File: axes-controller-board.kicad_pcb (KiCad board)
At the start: 2 copper layers, 135 parts, among them IC1 TPS5450QDDARQ1, IC2 ACS37800KMACTR-030B3-SPI, IC3 ACS37800KMACTR-030B3-SPI, IC4 ACS37800KMACTR-030B3-SPI, IC5 STM32H723ZGT6, J1 Conn_ST_STDC14, J10 Conn_01x08, J11 Conn_01x04, J12 Conn_01x08, J13 Conn_01x04, J14 Conn_01x08, J15 Conn_01x08, J16 Conn_01x04, J17 Conn_01x08, J18 Conn_01x08, J19 Conn_01x04, J2 Conn_01x03, J20 Conn_01x08, J21 Conn_01x08, J22 Conn_01x04, J23 Conn_01x08, J24 Conn_01x08, J25 Conn_01x04, J26 Conn_01x08, J27 Raspberry_Pi_2_3, J28 DC1, J29 DC2, J3 Conn_01x03, J30 DC3, J31 Conn_01x08, J32 Conn_01x08, J4 Conn_01x03, J5 DRIVER, J6 NTC, J7 DRIVER, J8 NTC, J9 Conn_01x08, SW1 RESET, U1 LM1117MP-3.3, U3 UA9637A, U5 UA9637A, U7 UA9637A, Y1 16MHz

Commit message: feat: setup groups pcb
steppers, micro, clock, current sensor - connector
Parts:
- moved C51 169.3 mm to (106.6, -64.5), turned to 90 degrees
- moved C53 169.3 mm to (152.6, -63.9), turned to 90 degrees
- moved C52 168.2 mm to (129.6, -64.2), turned to 90 degrees
- moved C11 163.5 mm to (217.2, 0.21), turned to -90 degrees
- moved C10 162.4 mm to (219.2, 0.21), turned to -90 degrees
- moved C15 161.6 mm to (213.8, -14.1), turned to -90 degrees
- moved L2 156.1 mm to (228.4, -5.54)
- moved R9 155.6 mm to (210.8, -14.1), turned to 90 degrees
- moved J16 155.5 mm to (149.3, -69.0), turned to 90 degrees
- moved R8 154.3 mm to (212.3, -14.1), turned to -90 degrees
- moved U1 152.9 mm to (218.4, 21.7)
- moved J13 152.3 mm to (125.9, -68.8), turned to 90 degrees
- moved J11 151.4 mm to (103.2, -68.6), turned to 90 degrees
- moved C13 150.1 mm to (212.5, -3.54), turned to 180 degrees
- moved C12 147.0 mm to (215.4, 0.06), turned to -90 degrees
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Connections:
- C13 pad 1: Net-(IC1-PH) -> /IBC
- C13 pad 2: Net-(D3-K) -> Net-(IC1-BOOT)
- D3 pad 1: Net-(D3-K) -> /IBC
- IC1 pad 1: Net-(D3-K) -> Net-(IC1-BOOT)
- IC1 pad 8: Net-(IC1-PH) -> /IBC
- J10 pad 1: GND -> +12V
- J10 pad 2: +3V3 -> GND
- J10 pad 7: GND -> +3V3
- J10 pad 8: +12V -> GND
- J14 pad 1: GND -> +12V
- J14 pad 2: +3V3 -> GND
- J14 pad 7: GND -> +3V3
- J14 pad 8: +12V -> GND
- J17 pad 1: GND -> +12V
- J17 pad 2: +3V3 -> GND
- J17 pad 7: GND -> +3V3
- J17 pad 8: +12V -> GND
- J20 pad 1: GND -> +12V
- J20 pad 2: +3V3 -> GND
- J20 pad 7: GND -> +3V3
- J20 pad 8: +12V -> GND
- J23 pad 1: GND -> +12V
- J23 pad 2: +3V3 -> GND
- J23 pad 7: GND -> +3V3
- J23 pad 8: +12V -> GND
- J26 pad 1: GND -> +12V
- J26 pad 2: +3V3 -> GND
- J26 pad 7: GND -> +3V3
- J26 pad 8: +12V -> GND
- J28 pad 1: /Sensors/DC_1_OUT -> /Sensors/DC_1_IN
- J28 pad 2: /Sensors/DC_1_IN -> /Sensors/DC_1_OUT
- J29 pad 1: /Sensors/DC_2_OUT -> /Sensors/DC_2_IN
- J29 pad 2: /Sensors/DC_2_IN -> /Sensors/DC_2_OUT
- J30 pad 1: /Sensors/DC_3_OUT -> /Sensors/DC_3_IN
- J30 pad 2: /Sensors/DC_3_IN -> /Sensors/DC_3_OUT
- L2 pad 1: Net-(D3-K) -> /IBC
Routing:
- net /MCU/OSC_OUT: track 0.00 -> 7.88 mm
- net /MCU/OSC_IN: track 1.81 -> 6.16 mm
- added copper zone on F.Cu, net +12V
- added copper zone on F.Cu, net /IBC
- added copper zone on F.Cu, net /Sensors/DC_1_IN
- added copper zone on F.Cu, net /Sensors/DC_1_OUT
- added copper zone on F.Cu, net /Sensors/DC_2_IN
- added copper zone on F.Cu, net /Sensors/DC_2_OUT
- added copper zone on F.Cu, net /Sensors/DC_3_IN
- added copper zone on F.Cu, net /Sensors/DC_3_OUT
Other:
- board text added: "+3V3"
- board text added: "+5V"

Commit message: fix: missing input power connector
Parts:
- added J33: DC1, TerminalBlock_Phoenix:TerminalBlock_Phoenix_MKDS-1,5-2-5.08_1x02_P5.08mm_Horizontal, F.Cu at (224.7, 6.96)
- moved JP2 148.0 mm to (79.5, -43.2)
- moved C39 108.6 mm to (270.7, 139.2), turned to 180 degrees
- moved C34 93.1 mm to (254.3, 139.1), turned to 180 degrees
- moved C33 80.2 mm to (238.5, 139.1), turned to 180 degrees
- moved J2 76.8 mm to (96.3, 18.9)
- moved J3 76.8 mm to (101.0, 18.9)
- moved J4 76.8 mm to (105.6, 18.9)
- moved C32 28.9 mm to (198.3, 94.3)
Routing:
- net GND: track 35.0 -> 41.5 mm
- net +3V3: track 42.8 -> 48.9 mm

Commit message: feat: sbroglio encoders drivers
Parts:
- moved R50 70.6 mm to (168.0, 170.2), turned to 180 degrees
- moved R49 70.0 mm to (168.0, 167.1), turned to 180 degrees
- moved R38 69.8 mm to (158.0, 156.6), turned to -90 degrees
- moved R52 68.8 mm to (158.2, 170.7), turned to -90 degrees
- moved C45 68.5 mm to (168.0, 171.8), turned to 180 degrees
- moved R51 68.3 mm to (158.2, 167.6), turned to 90 degrees
- moved U7 68.1 mm to (162.7, 169.5)
- moved R39 68.0 mm to (156.4, 156.7), turned to -90 degrees
- moved C44 68.0 mm to (168.0, 168.7), turned to 180 degrees
- moved R53 66.9 mm to (156.7, 170.6), turned to -90 degrees
- moved C49 64.8 mm to (155.1, 170.6), turned to 90 degrees
- moved C42 63.5 mm to (154.9, 156.7), turned to 90 degrees
- moved R40 62.9 mm to (156.4, 153.6), turned to -90 degrees
- moved C54 62.5 mm to (145.9, -76.3)
- moved C55 62.5 mm to (171.8, -76.2)
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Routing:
- net Net-(IC1-VSENSE): track 0.00 -> 19.8 mm
- net Net-(IC1-BOOT): track 0.00 -> 4.65 mm
- net /MCU/MY1_A: track 0.00 -> 3.13 mm
- net /MCU/MY2_B: track 0.00 -> 3.11 mm
- net /MCU/MY2_A: track 0.00 -> 3.11 mm
- net /MCU/MY1_B: track 0.00 -> 3.11 mm
- net /MCU/MX_A: track 0.00 -> 3.10 mm
- net /MCU/MX_B: track 0.00 -> 3.08 mm
- net Net-(U3-OUT1): track 0.00 -> 2.23 mm
- net /Sensors/M1_B-: track 0.00 -> 2.20 mm
- net /Sensors/M2_A+: track 0.00 -> 2.19 mm
- net /Sensors/M3_B-: track 0.00 -> 2.19 mm
- net Net-(U5-OUT1): track 0.00 -> 2.19 mm
- net Net-(U7-OUT1): track 0.00 -> 2.19 mm
- net Net-(U3-OUT2): track 0.00 -> 2.17 mm
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
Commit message: feat: rasp, supply and micro setup on pcb, missing stepper motors connectors
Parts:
- moved D5 240.8 mm to (143.7, 135.3)
- moved R10 240.8 mm to (142.1, 135.3)
- moved R11 240.8 mm to (142.1, 138.4)
- moved D6 240.8 mm to (143.7, 138.4)
- moved J1 233.6 mm to (128.1, 153.3)
- moved SW1 229.0 mm to (117.5, 152.1), turned to 90 degrees
- moved C6 225.9 mm to (120.3, 149.5), turned to 90 degrees
- moved D7 225.1 mm to (120.2, 152.4), turned to -90 degrees
- moved J4 213.7 mm to (257.1, 169.6), turned to 90 degrees
- moved J3 213.7 mm to (262.5, 158.8)
- moved J5 202.3 mm to (331.0, 77.5)
- moved J31 202.3 mm to (310.0, 88.4)
- moved J32 202.3 mm to (310.0, 99.2)
- moved J6 202.3 mm to (321.7, 77.5)
- moved J7 202.3 mm to (335.6, 77.5)
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
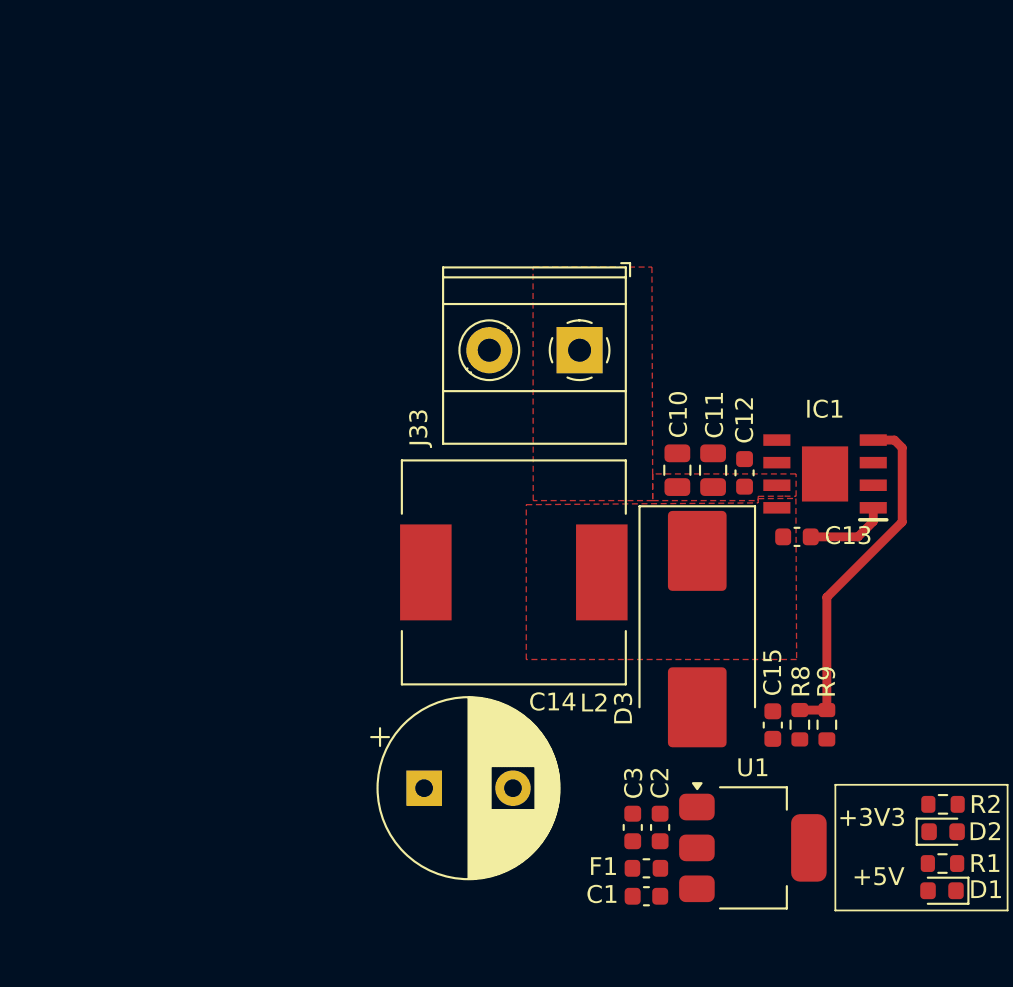
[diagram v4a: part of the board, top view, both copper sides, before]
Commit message: fix: dcdc layout according to datasheet
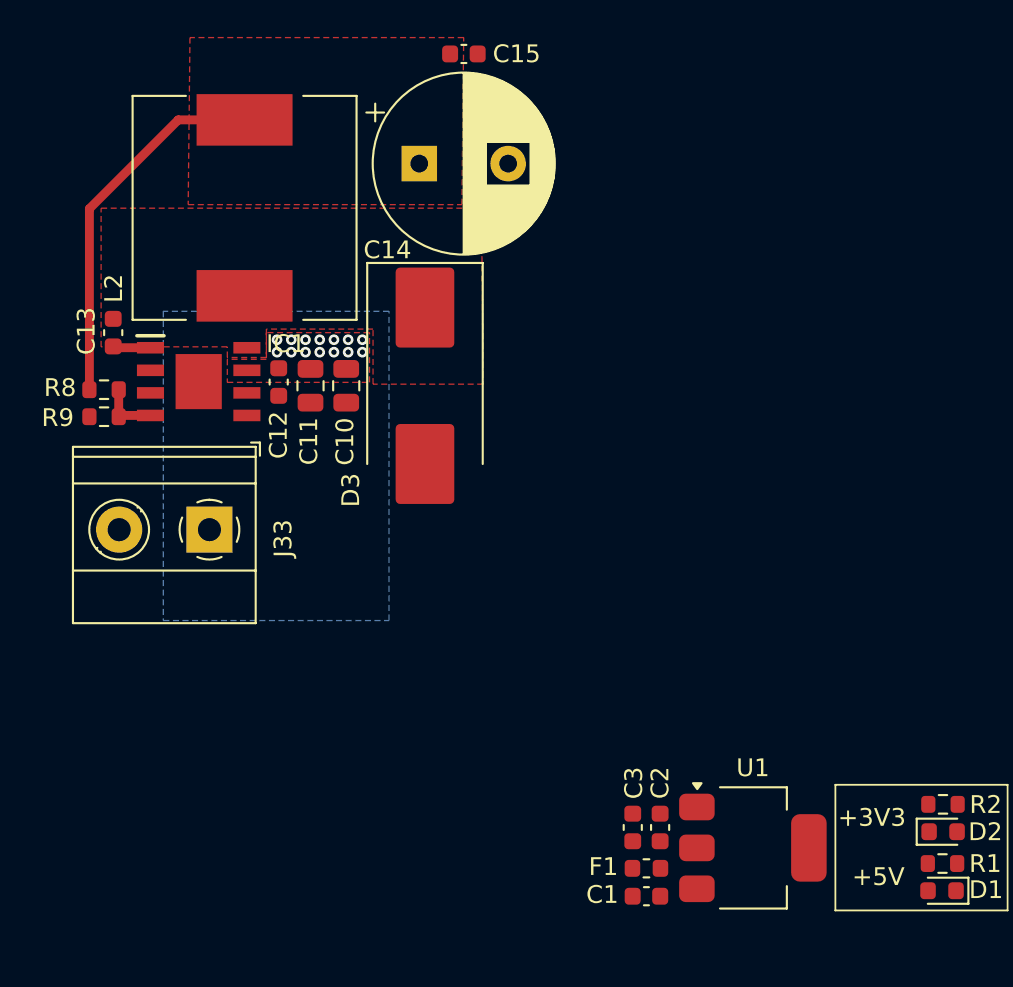
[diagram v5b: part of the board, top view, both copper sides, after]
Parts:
- moved R9 44.2 mm to (41.5, 63.4), turned to 180 degrees
- moved R8 43.4 mm to (41.5, 61.9), turned to 0 degrees
- moved C15 41.6 mm to (61.7, 43.0), turned to 0 degrees
- moved C13 40.1 mm to (42.0, 58.7), turned to -90 degrees
- moved IC1 35.6 mm to (46.8, 61.4), turned to 0 degrees
- moved C14 35.1 mm to (59.2, 49.2)
- moved C12 26.7 mm to (51.3, 61.5), turned to -90 degrees
- moved L2 25.5 mm to (49.4, 51.6), turned to 90 degrees
- moved J33 23.1 mm to (47.4, 69.8)
- moved C11 23.1 mm to (53.1, 61.7), turned to -90 degrees
- moved D3 20.5 mm to (59.5, 61.7)
- moved C10 19.2 mm to (55.1, 61.7), turned to -90 degrees
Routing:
- net +5V: track 0.00 -> 21.0 mm
- net Net-(IC1-VSENSE): track 19.8 -> 3.33 mm
- net Net-(IC1-BOOT): track 4.65 -> 2.13 mm
- net +12V: vias 0 -> 14
- added copper zone on B.Cu, net +12V
- added copper zone on F.Cu, net +5V

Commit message: feat: 3d models and first draft pcb edge cuts
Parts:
- J27: moved to B.Cu
- moved J32 171.5 mm to (145.9, 149.0)
- moved J31 157.0 mm to (165.1, 149.0)
- moved C45 152.9 mm to (182.8, 143.8), turned to 90 degrees
- moved R50 150.9 mm to (184.3, 143.8), turned to 90 degrees
- moved C44 149.0 mm to (185.8, 143.8), turned to 90 degrees
- moved R49 147.1 mm to (187.4, 143.8), turned to 90 degrees
- moved U7 146.6 mm to (185.1, 138.5), turned to -90 degrees
- moved R52 145.5 mm to (183.9, 134.0), turned to 180 degrees
- moved R53 144.7 mm to (183.9, 132.5), turned to 180 degrees
- moved C49 143.9 mm to (183.9, 130.9), turned to 0 degrees
- moved R51 141.6 mm to (186.9, 134.0), turned to 0 degrees
- moved R54 140.7 mm to (186.9, 132.5), turned to 180 degrees
- moved C47 140.6 mm to (188.7, 136.3), turned to -90 degrees
- moved C50 139.9 mm to (186.9, 130.9), turned to 180 degrees
- moved C38 137.2 mm to (194.9, 143.8), turned to 90 degrees
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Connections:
- J33 pad 1: +12V -> GND
- J33 pad 2: GND -> +12V
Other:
- board outline added: 184.6 x 102.9 mm

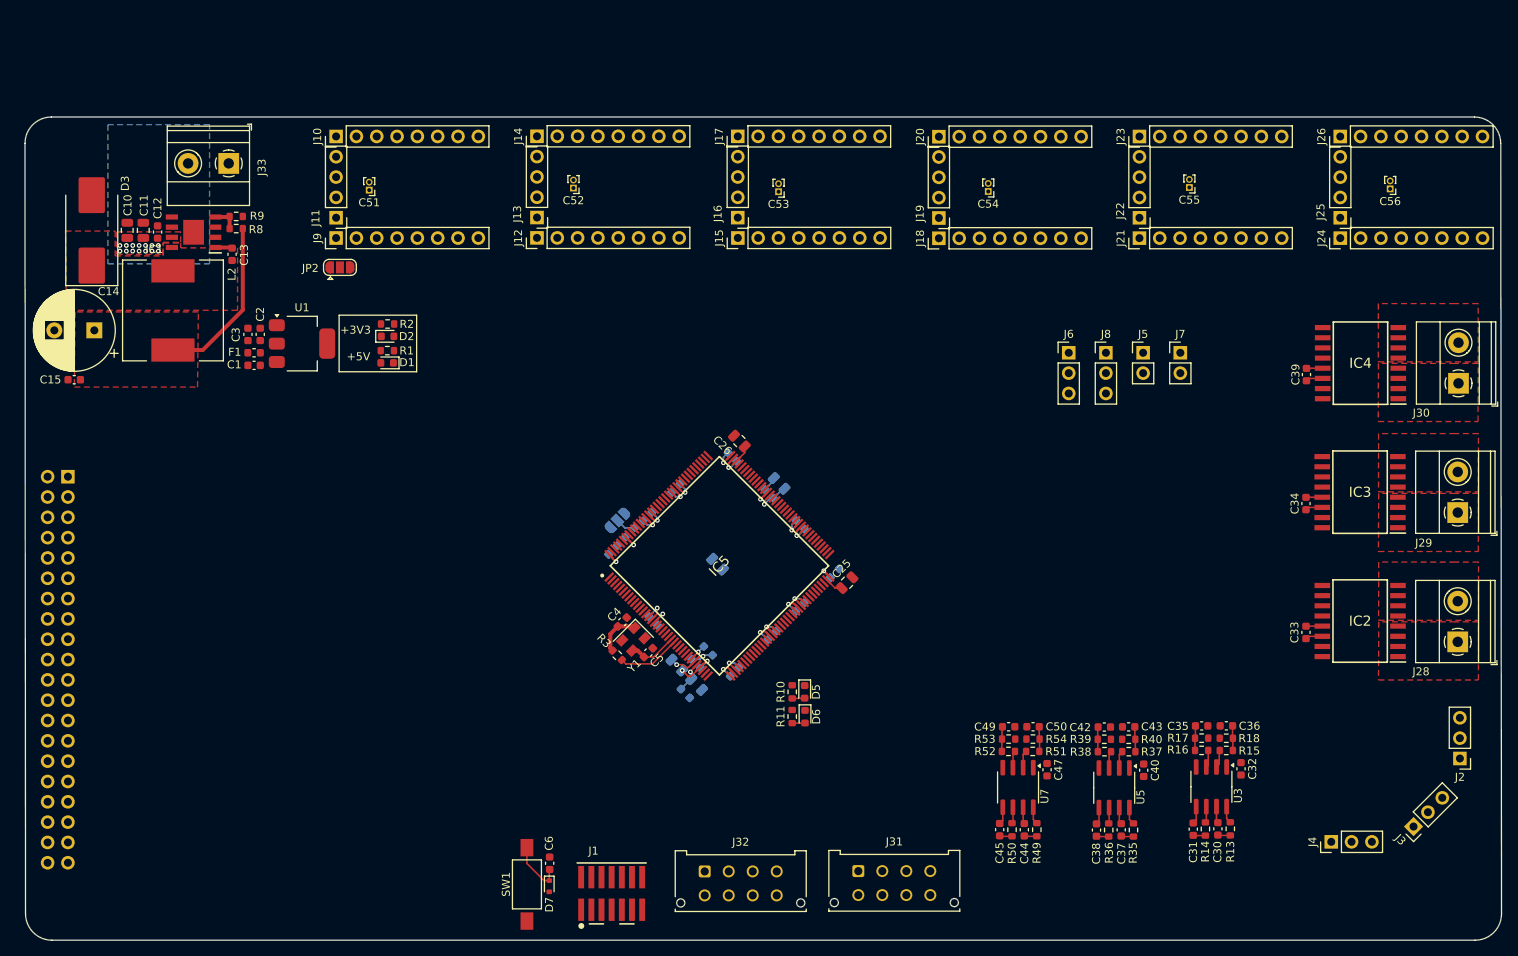
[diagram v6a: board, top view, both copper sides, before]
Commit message: fix: connectors and pcb layout
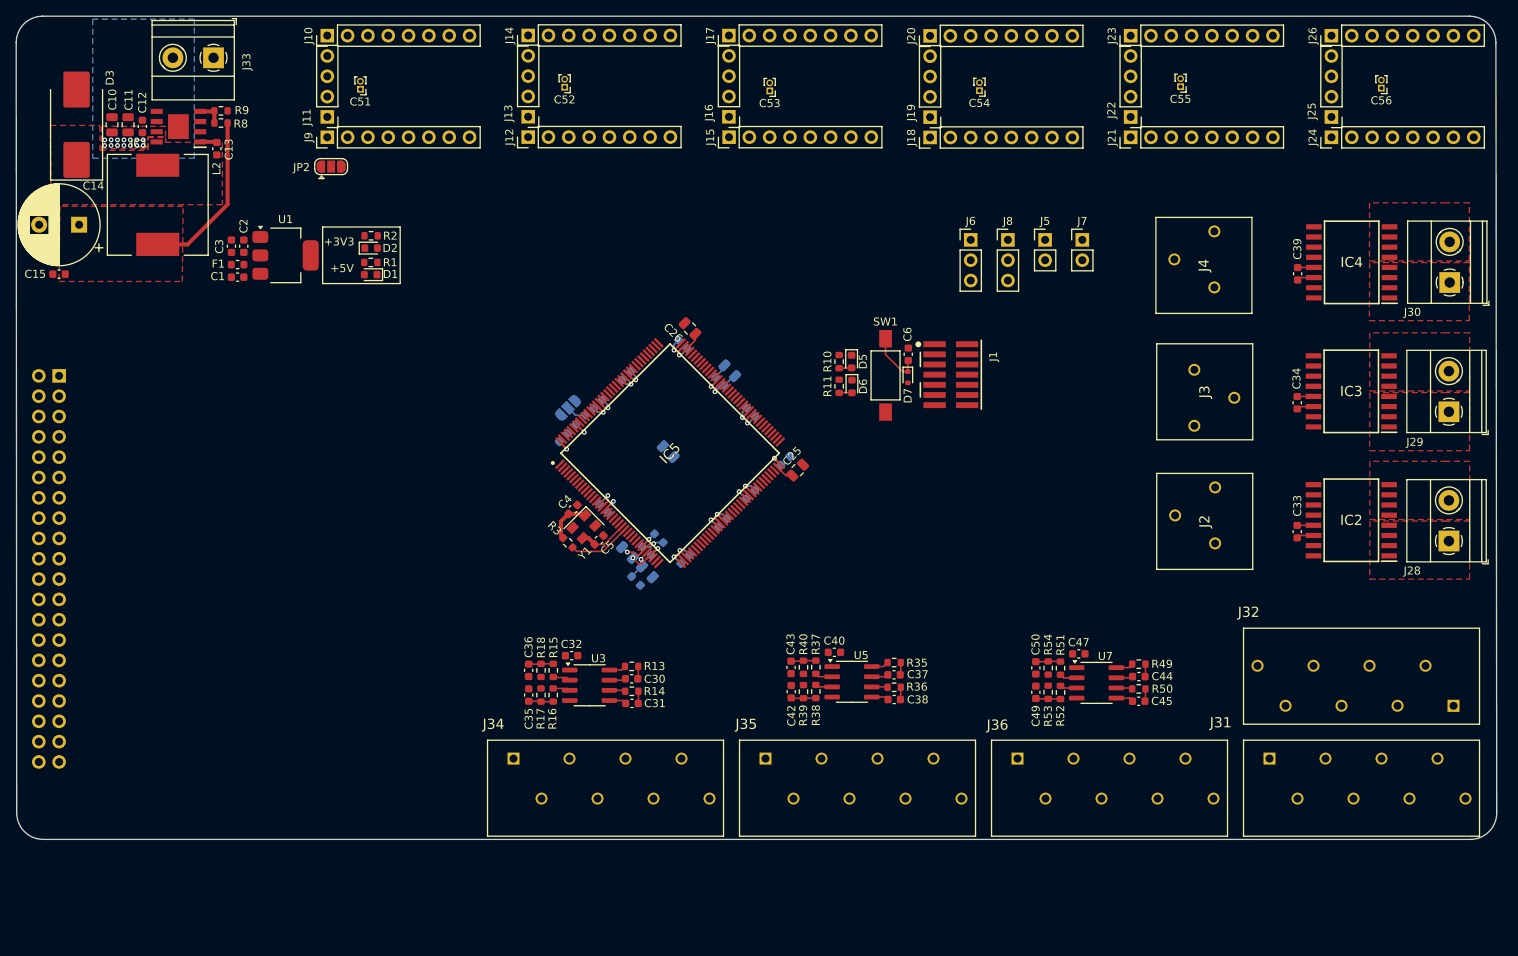
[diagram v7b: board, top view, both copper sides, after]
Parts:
- added J34: Conn_01x08, Local:1985250, F.Cu at (122.0, 134.9)
- added J35: Conn_01x08, Local:1985250, F.Cu at (153.5, 134.9)
- added J36: Conn_01x08, Local:1985250, F.Cu at (185.0, 134.9)
- J2, J3, J4: footprint Connector_PinHeader_2.54mm:PinHeader_1x03_P2.54mm_Vertical -> Local:1985205
- J31, J32: footprint Connector_Molex:Molex_Micro-Fit_3.0_43045-0812_2x04_P3.00mm_Vertical -> Local:1985250
- moved J32 95.9 mm to (239.5, 128.3), turned to 180 degrees
- moved C36 87.5 mm to (123.9, 123.9), turned to -90 degrees
- moved R18 86.1 mm to (125.4, 123.9), turned to -90 degrees
- moved C32 84.9 mm to (129.3, 122.0), turned to 0 degrees
- moved R15 84.7 mm to (127.0, 123.9), turned to 90 degrees
- moved C35 84.2 mm to (123.9, 127.0), turned to 90 degrees
- moved R17 82.8 mm to (125.4, 127.0), turned to -90 degrees
- moved R16 81.3 mm to (127.0, 127.0), turned to -90 degrees
- moved U3 78.8 mm to (131.5, 125.7), turned to 0 degrees
- moved SW1 77.8 mm to (168.5, 87.0)
- moved C6 77.8 mm to (171.3, 84.4)
- moved D7 77.8 mm to (171.3, 87.2)
- moved R13 77.5 mm to (136.8, 123.4), turned to 180 degrees
- moved J1 77.5 mm to (176.7, 86.9), turned to -90 degrees
- moved C30 75.6 mm to (136.8, 124.9), turned to 180 degrees
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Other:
- board size 184.6 x 102.9 mm -> 185.1 x 102.9 mm

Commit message: feat: gnd zones
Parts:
- moved J2 2.00 mm to (208.4, 103.2)
- moved J4 1.60 mm to (208.4, 74.8)
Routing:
- net /Sensors/M3_B-: track 2.19 -> 23.3 mm
- net /Sensors/M1_B-: track 2.20 -> 23.0 mm
- net /Sensors/M2_B-: track 2.16 -> 22.8 mm
- net /Sensors/M3_A-: track 2.10 -> 21.8 mm
- net /Sensors/M1_A-: track 2.08 -> 21.8 mm
- net /Sensors/M2_A-: track 2.11 -> 21.7 mm
- net /Sensors/M3_B+: track 2.03 -> 18.9 mm
- net /Sensors/M1_B+: track 2.02 -> 18.9 mm
- net /Sensors/M2_B+: track 2.00 -> 18.5 mm
- net /Sensors/M1_A+: track 2.14 -> 17.2 mm
- net /Sensors/M3_A+: track 2.17 -> 17.0 mm
- net /Sensors/M2_A+: track 2.19 -> 16.9 mm
- added copper zone on B.Cu, net GND
- added copper zone on F.Cu, net GND
